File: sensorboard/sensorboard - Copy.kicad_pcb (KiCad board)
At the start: 4 copper layers, 100 x 50 mm, 244 parts, among them J1 Conn_01x03, J10 Conn_01x02_Male, J11 Conn_01x05_Male, J12 Conn_01x03, J13 Conn_01x03, J14 USB_C_Receptacle_USB2.0, J2 Conn_01x03, J3 Conn_01x03, J4 Conn_01x03, J5 Conn_01x03, J6 Conn_01x03, J7 Conn_01x03, J8 Conn_01x03, J9 Conn_01x02_Male, Q1 MMDT2222A, U1 ESP32-PICO-D4, U10 MAX31856, U11 MAX31856, U12 RT9025-25GSP, U13 ADS1219, U14 ADS1219, U15 ADS1219, U16 MAX31856, U17 MAX31856, U18 MAX31856, U19 LTC4411, U2 LTC4411, U20 SN65HVD230, U3 TPS61092RSAR, U4 MAX31856, U5 MAX31856, U6 MAX31856, U7 MAX31856, U8 CP2102-GMR-QFN28, U9 MAX31856

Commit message: rearrange CAN, USB port and new copies
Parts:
- C1, C2, C3: value 1nF -> 0.1uF
- moved U15 147.7 mm to (189.1, 46.3), turned to 180 degrees
- moved C58 146.8 mm to (191.5, 42.7)
- moved Q1 145.9 mm to (152.1, 61.8), turned to 90 degrees
- moved R1 145.2 mm to (149.8, 61.4), turned to 90 degrees
- moved R2 144.9 mm to (152.6, 59.3)
- moved TP6 141.2 mm to (155.5, 50.8)
- moved R5 140.0 mm to (105.0, 50.4), turned to -90 degrees
- moved R31 137.3 mm to (183.7, 46.7), turned to 180 degrees
- moved C1 134.9 mm to (102.3, 51.0), turned to 180 degrees
- moved J9 134.2 mm to (102.3, 48.4), turned to 180 degrees
- moved U14 133.8 mm to (167.8, 43.3), turned to 180 degrees
- moved C57 127.1 mm to (164.5, 38.7), turned to -90 degrees
- moved R30 122.0 mm to (162.2, 43.5), turned to 180 degrees
- moved C3 119.5 mm to (102.4, 58.9), turned to 180 degrees
- moved TP5 118.7 mm to (154.4, 52.6), turned to -90 degrees
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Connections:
- TP1 pad 1: /CS9 -> /CS3
- TP10 pad 1: /CS6 -> /CS7
- TP11 pad 1: /C55 -> /CS5
- TP12 pad 1: /CS4 -> /CS9
- TP13 pad 1: /CS3 -> /CS4
- TP19 pad 1: /CS2 -> /CS8
- TP2 pad 1: /CS8 -> /CS2
- TP21 pad 1: /CS0 -> /CS6
- TP22 pad 1: /CAN_TX -> /CAN_RX
- TP23 pad 1: /CAN_RX -> /CAN_TX
- TP8 pad 1: /BOOT -> /CS0
- TP9 pad 1: /CS7 -> /BOOT
- U1 pad 12: /CAN_TX -> unconnected-(U1-Pad12)
- U1 pad 13: /CAN_RX -> unconnected-(U1-Pad13)
- U1 pad 14: /CS2 -> /CS8
- U1 pad 16: /CS0 -> /CS6
- U1 pad 17: /CS4 -> /CS9
- U1 pad 18: /CS6 -> /CS7
- U1 pad 20: /C55 -> /CS5
- U1 pad 21: /CS3 -> /CS4
- U1 pad 22: /LED -> /CS3
- U1 pad 23: /BOOT -> /CS0
- U1 pad 24: unconnected-(U1-Pad24) -> /CS2
- U1 pad 25: unconnected-(U1-Pad25) -> /CAN_RX
- U1 pad 27: unconnected-(U1-Pad27) -> /CAN_TX
- U1 pad 28: /CS8 -> unconnected-(U1-Pad28)
- U1 pad 29: /CS7 -> /BOOT
- U1 pad 34: /CS9 -> /LED
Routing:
- net +3V3: track 49.9 -> 347.3 mm, vias 3 -> 17
- net /MOSI: track 2.34 -> 162.8 mm, vias 1 -> 12
- net /MISO: track 2.37 -> 131.5 mm, vias 1 -> 11
- net /SCLK: track 2.07 -> 119.9 mm, vias 1 -> 11
- net /SDA: track 0.00 -> 72.4 mm, vias 0 -> 4
- net /EN: track 0.00 -> 69.5 mm, vias 0 -> 4
- net /SCL: track 0.00 -> 69.0 mm, vias 0 -> 5
- net /BOOT: track 0.00 -> 60.8 mm, vias 0 -> 2
- net /CAN_RX: track 0.00 -> 53.1 mm, vias 0 -> 1
- net /CAN_TX: track 0.00 -> 48.5 mm, vias 0 -> 1
- net +5V: track 0.00 -> 44.5 mm
- net /CS7: track 0.00 -> 41.3 mm
- net /CS5: track 0.00 -> 40.5 mm
- net VBUS: track 34.2 -> 71.8 mm, vias 0 -> 4
- net /CS9: track 0.00 -> 33.7 mm
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
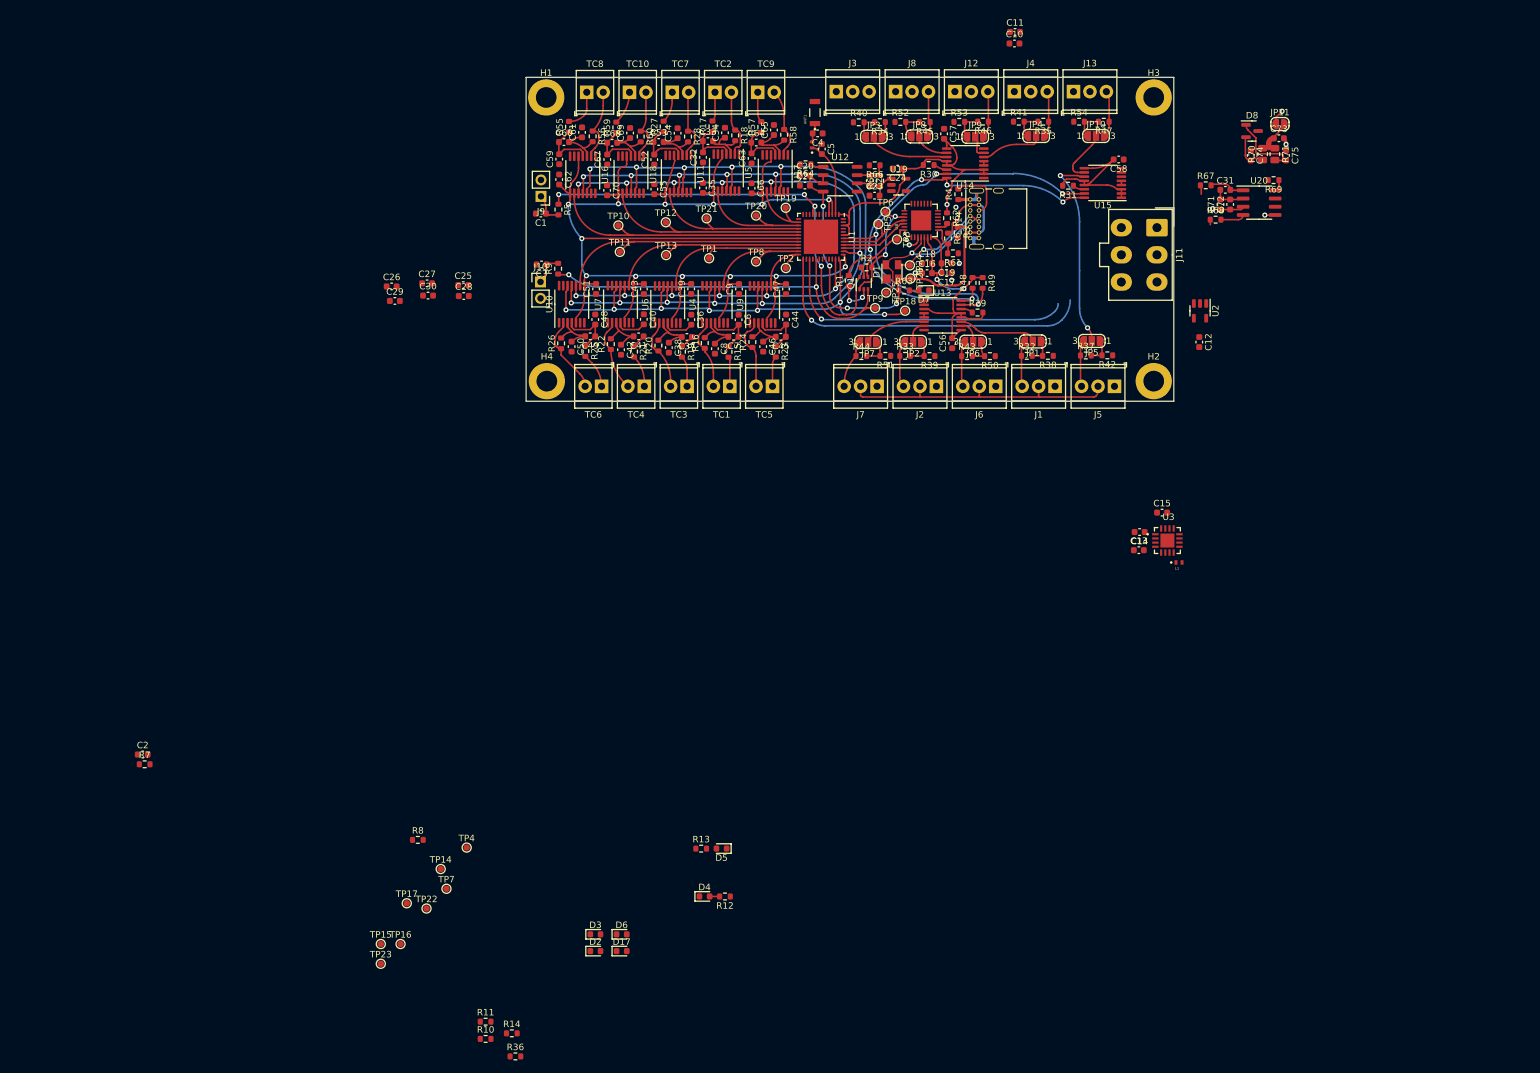
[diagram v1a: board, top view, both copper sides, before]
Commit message: Change 3.3V, added curved edges
changed the copy, added keepout for UFL connector
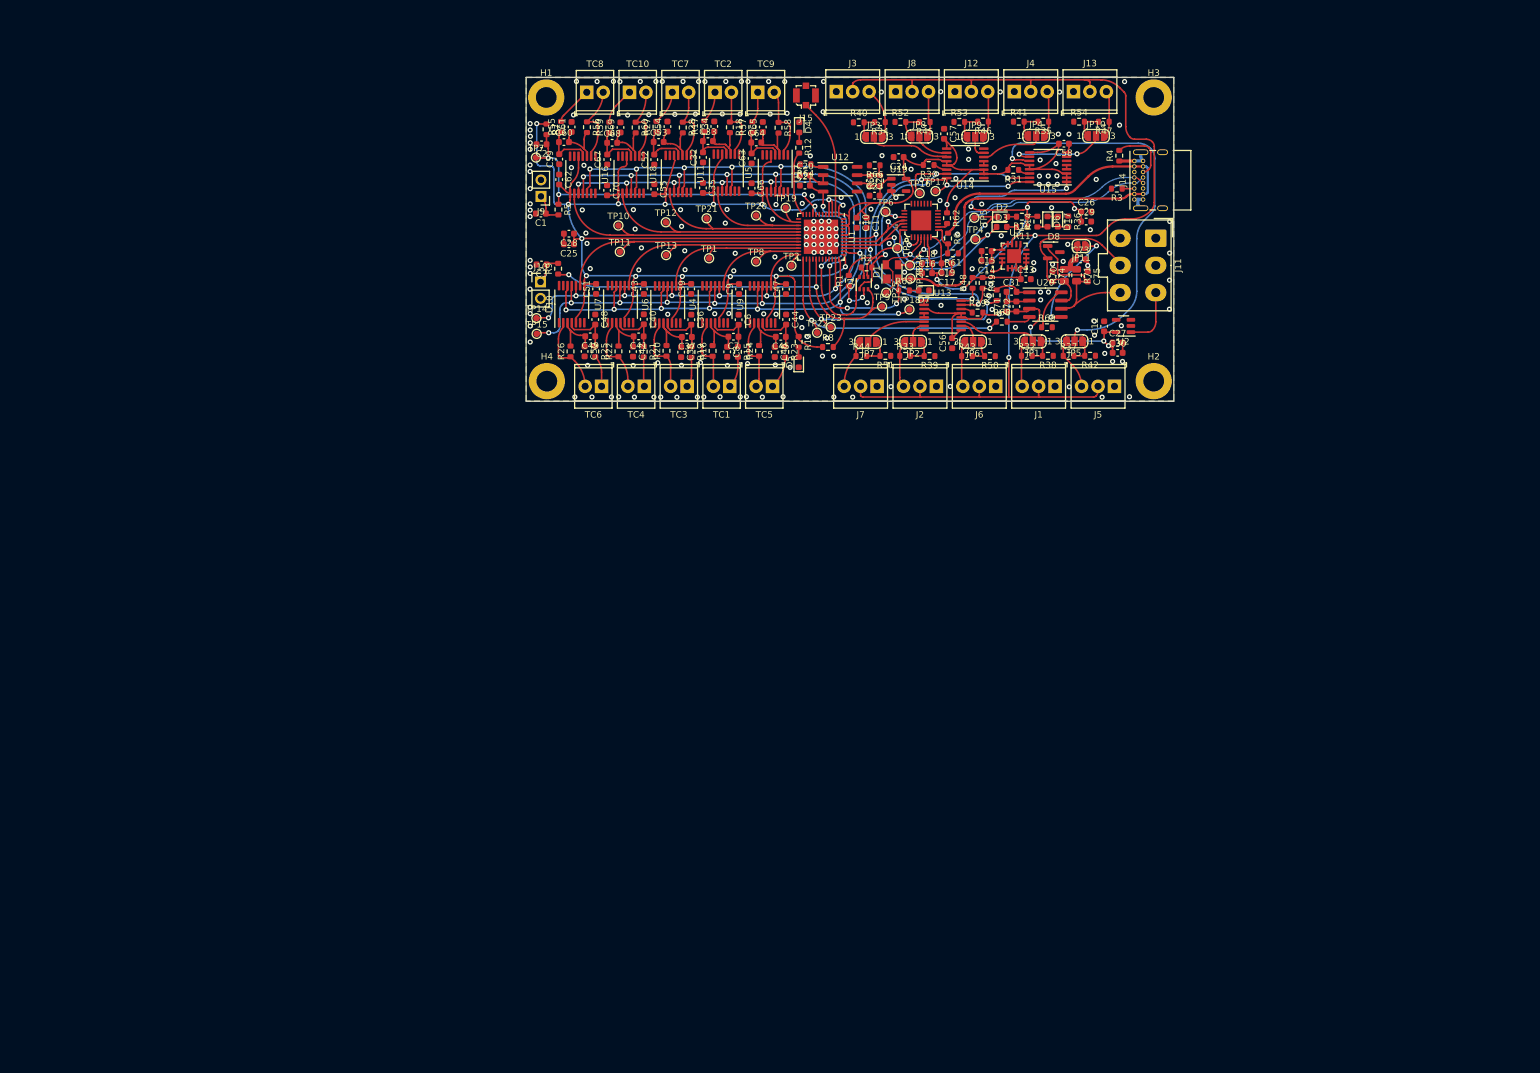
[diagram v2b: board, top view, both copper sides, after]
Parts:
- removed ANT1: AMCA31-2R450G-S1F-T3, iclr:ANT_AMCA31-2R450G-S1F-T3
- removed C4: 1.2pF, Capacitor_SMD:C_0603_1608Metric
- removed C5: 1.5pF, Capacitor_SMD:C_0603_1608Metric
- removed L2: LQG15WZ1N8B02D, iclr:INDC1006X60N
- added J15: Conn_Coaxial, Connector_Coaxial:U.FL_Molex_MCRF_73412-0110_Vertical, F.Cu at (143.2, 32.8)
- moved R36 154.6 mm to (183.7, 52.2), turned to -90 degrees
- moved R10 151.6 mm to (176.5, 51.5), turned to 180 degrees
- moved R14 149.3 mm to (178.9, 52.3), turned to 90 degrees
- moved R11 148.0 mm to (176.5, 53.1), turned to 180 degrees
- moved TP16 140.9 mm to (160.8, 47.9)
- moved TP17 136.9 mm to (163.2, 47.6)
- moved D17 131.2 mm to (182.1, 52.3), turned to -90 degrees
- moved D2 129.6 mm to (173.5, 51.5)
- moved D6 128.2 mm to (180.5, 52.3), turned to -90 degrees
- moved D3 126.0 mm to (173.4, 53.1)
- moved TP4 122.4 mm to (169.4, 55.0)
- moved TP23 120.4 mm to (147.0, 68.6)
- moved D4 119.6 mm to (142.2, 37.7), turned to -90 degrees
- moved R12 116.2 mm to (142.2, 40.9), turned to 90 degrees
- moved R7 116.0 mm to (103.1, 38.0), turned to -90 degrees
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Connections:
- C13 pad 1: unconnected-(C13-Pad1) -> +3V3
- C15 pad 1: unconnected-(C15-Pad1) -> +5V
- U1 pad 12: unconnected-(U1-Pad12) -> /LED
- U1 pad 34: /LED -> unconnected-(U1-Pad34)
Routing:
- net +3V3: track 347.3 -> 496.4 mm, vias 17 -> 26
- net +5V: track 44.5 -> 173.7 mm, vias 0 -> 2
- net VBUS: track 71.8 -> 134.3 mm
- net /analogueI2C/AIN8: track 30.5 -> 63.5 mm
- net /usb/Data+: track 24.8 -> 54.3 mm
- net /RXD: track 13.1 -> 40.0 mm, vias 0 -> 2
- net /usb/Data-: track 19.4 -> 46.3 mm
- net /TXD: track 10.7 -> 36.4 mm, vias 0 -> 2
- net /CAN_HIGH: track 5.54 -> 26.6 mm
- net /EN: track 69.5 -> 87.0 mm, vias 4 -> 5
- net GND: track 20.8 -> 38.3 mm, vias 6 -> 202
- net /CAN_LOW: track 11.8 -> 25.8 mm
- net /CAN/Vref: track 3.95 -> 17.1 mm
- net /CAN_RX: track 53.1 -> 41.2 mm, vias 1 -> 2
- net /LED: track 0.00 -> 10.0 mm
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- added copper zone on In1.Cu, net +3V3
- added copper zone on In2.Cu, net +3V3
- added copper zone on B.Cu, net GND
- added copper zone on F.Cu, net GND
